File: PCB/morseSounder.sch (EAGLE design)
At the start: 51 parts, among them IC1 LM386N-1, IC2 LM324N, IC3 MAT-02H, Q1 2N3904

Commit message: Added avr based keyer and key input stages
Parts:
- added IC4: AVR-MEGA8-PPTH, SparkFun:AVR-MEGA8-PPTH
- added J1: AVR_SPI_PRG_6PTH, SparkFun:AVR_SPI_PRG_6PTH
- added JP1, JP3, JP4: JUMPER-3SMD, SparkFun:JUMPER-3SMD
- added LED1, LED2, LED3: (no value), SparkFun:LED-3MM-NO_SILK
- added OK2, OK3: 4N35, optocoupler:4N35
- added R27, R28, R29: 750, SparkFun:RESISTOR0805-RES
- added S1: (no value), SparkFun:SWITCH-SPSTSMD2
- added U$4: MOUNTSPKR_20*40, morseSounder:MOUNTSPKR_20*40
- added U$6: P082DTH, morseSounder:P082DTH
- added X1: (no value), con-molex:KK-156-2
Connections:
- net N$10 renamed KEY_IN
- new net ADC_RATE: IC4.PC1(ADC1), U$6G$1.S
- new net ADC_WEIGHT: IC4.PC0(ADC0), U$6G$2.S
- new net AVR_DASH: IC4.PC3(ADC3)
- new net AVR_DOT: IC4.PC2(ADC2)
- new net AVR_KEY_DASH: OK3.COL
- new net AVR_KEY_DOT: OK2.COL
- new net AVR_KEY_MODE: IC4.PC5(ADC5/SCL), S1.P
- new net AVR_KEY_OUT: IC4.PC4(ADC4/SDA), JP4.1
- new net AVR_MISO: IC4.PB4(MISO), J1.1
- new net AVR_MOSI: IC4.PB3(MOSI/OC2), J1.4
- new net AVR_RESET: IC4.PC6(/RESET), J1.5
- new net AVR_RX: IC4.PD0(RXD)
- new net AVR_SCK: IC4.PB5(SCK), J1.3
- new net AVR_TX: IC4.PD1(TXD)
- new net AVR_VCC: IC4.AREF, IC4.AVCC, IC4.VCC@1, J1.2, R28.2, R29.2, U$6G$1.E, U$6G$2.E
- new net KEY_DASH: JP3.3, OK3.C, U$1.RING
- new net KEY_DOT: JP3.1, OK2.C, U$1.TIP
- new net KEY_INPUT: JP1.1, JP3.2
- new net N$10: LED1.C, OK1.A
- new net N$28: U$2.TN, X1-1.S
- new net N$29: LED3.A, R29.1
- new net N$30: JP4.2, R27.2
- new net N$31: JP1.2, OK1.C
- new net N$32: LED1.A, R27.1
- new net N$33: LED2.A, R28.1
- new net N$34: LED2.C, OK3.A
- new net N$35: LED3.C, OK2.A
- net +12V: now also JP4.3
- net GND: now also IC4.AGND, IC4.GND@1, J1.6, JP1.3, OK2.EMI, OK3.EMI, S1.S, U$6G$1.A, U$6G$2.A, X1-2.S
- net N$2: now also U$2.RING
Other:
- note added: "AVR opto isolators"
- note added: "Internal speaker connector"
- note added: "Keyer IC and programming header"
- note added: "Keyer controls"
- note added: "Level translator and key input select"
- note added: "Rate"
- note added: "Weight"
- note added: "for keyer"
- note added: "for non keyer"
- note added: "non keyer Input selection"
- moved on the sheet: C1, C10, C11, C12, C13, C14, C15, C16, C2, C3, C4, C5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

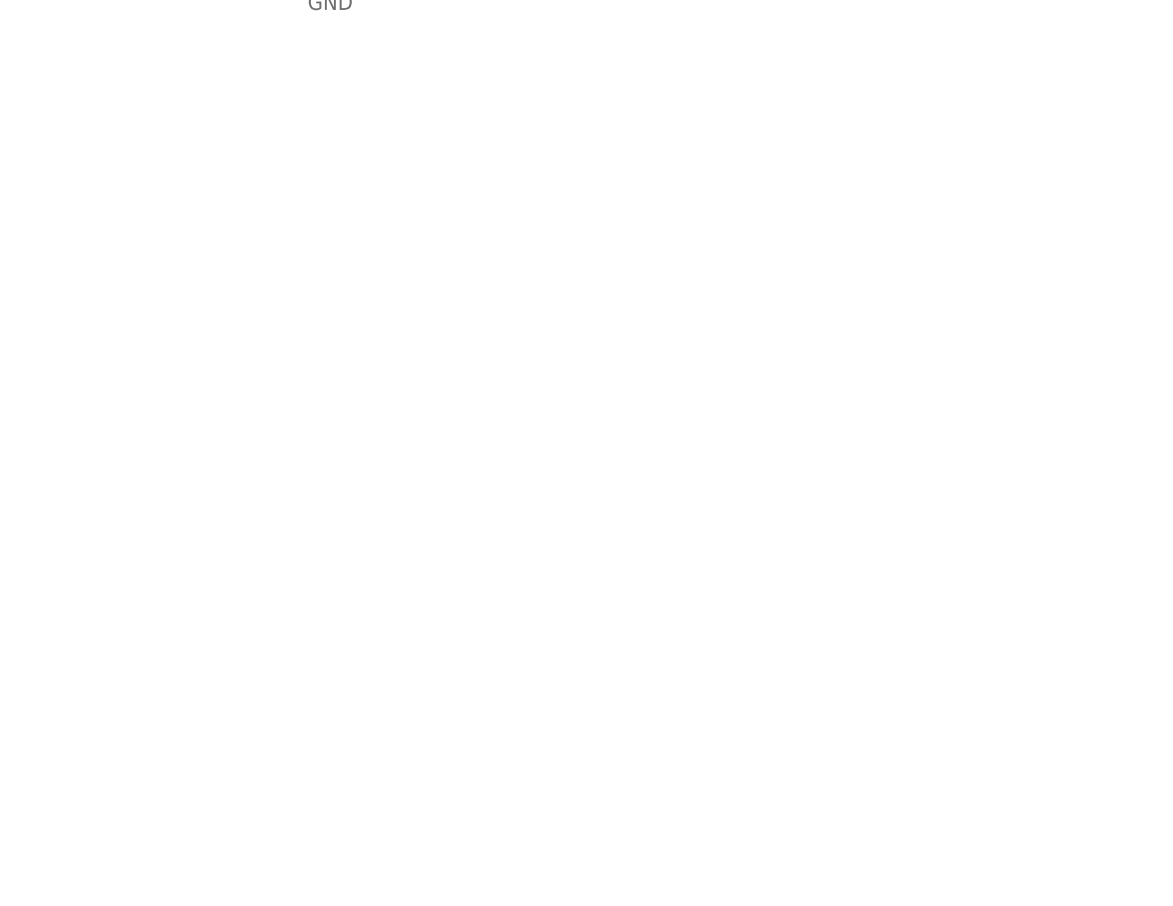
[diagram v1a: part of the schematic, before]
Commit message: Added power supply circuitry
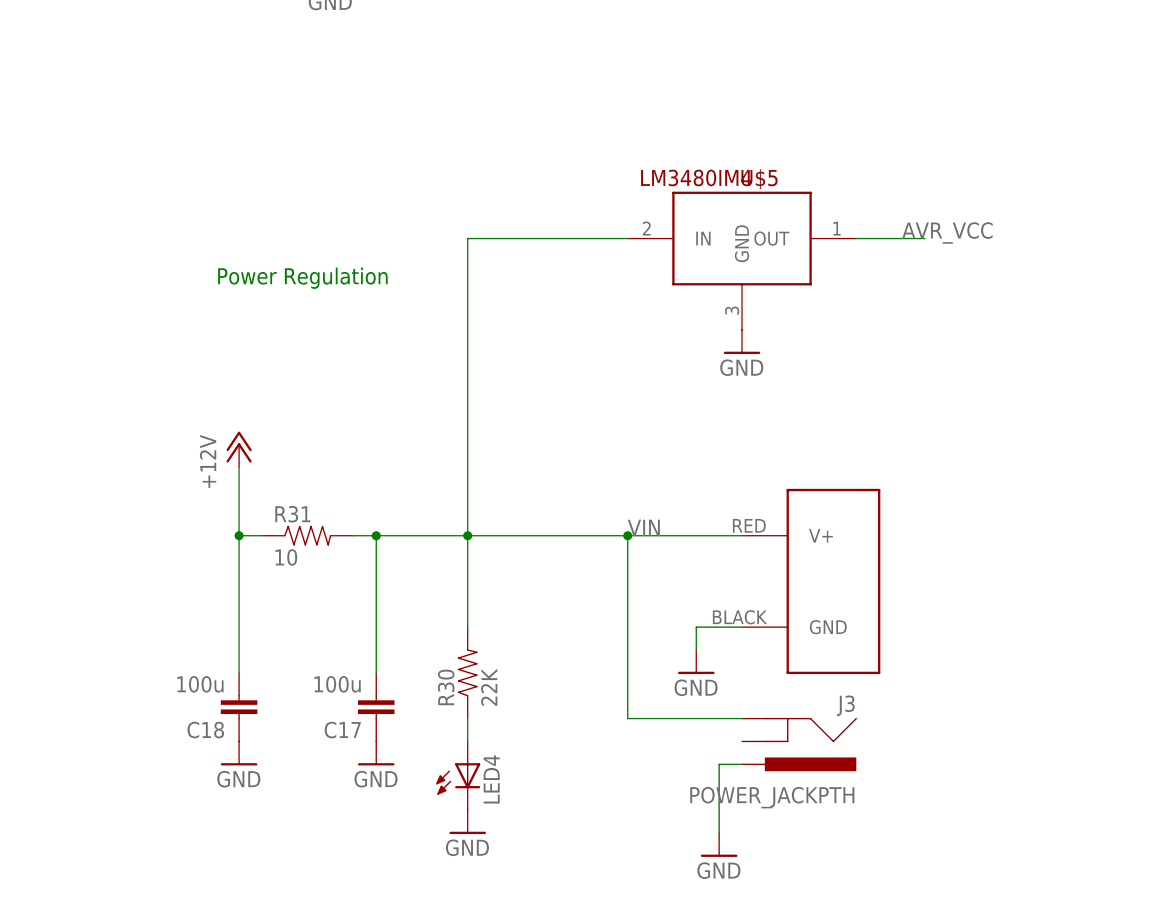
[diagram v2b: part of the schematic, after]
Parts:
- added C17, C18: 100u, SparkFun:CAP0805
- added J2: POWERPOLE_POWER25A_HORIZONTAL_G2, powerpoles:POWERPOLE_POWER25A_HORIZONTAL_G2
- added J3: POWER_JACKPTH, SparkFun:POWER_JACKPTH
- added LED4: (no value), SparkFun:LED-3MM-NO_SILK
- added R30: 22K, SparkFun:RESISTOR0805-RES
- added R31: 10, SparkFun:RESISTOR0805-RES
- added U$5: LM3480IM4, SparkFun-PowerIC:LM3480IM4
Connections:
- new net N$36: LED4.A, R30.1
- new net VIN: C17.2, J2.V+, J3.GND, R30.2, R31.2, U$5.IN
- net +12V: now also C18.2, R31.1
- net AVR_VCC: now also U$5.OUT
- net GND: now also C17.1, C18.1, J2.GND, J3.PWR, LED4.C, U$5.GND
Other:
- note added: "Power Regulation"
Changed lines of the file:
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@@
 <layer number="56" name="wert" color="7" fill="1" visible="no" active="no"/>
 <layer number="57" name="tCAD" color="7" fill="1" visible="no" active="no"/>
+<layer number="90" name="Modules" color="5" fill="1" visible="yes" active="yes"/>
 <layer number="91" name="Nets" color="2" fill="1" visible="yes" active="yes"/>
 <layer number="92" name="Busses" color="1" fill="1" visible="yes" active="yes"/>
@@
 <layer number="251" name="SMDround" color="12" fill="11" visible="no" active="no"/>
 <layer number="254" name="cooling" color="7" fill="1" visible="no" active="yes"/>
+<layer number="255" name="routoute" color="7" fill="1" visible="yes" active="yes"/>
 </layers>
 <schematic xreflabel="%F%N/%S.%C%R" xrefpart="/%S.%C%R">
@@
 <part name="S1" library="SparkFun" deviceset="SWITCH-SPST" device="SMD2"/>
 <part name="GND24" library="supply1" deviceset="GND" device=""/>
+<part name="U$5" library="SparkFun-PowerIC" deviceset="LM3480IM4" device=""/>
+<part name="J2" library="powerpoles" deviceset="POWERPOLE_POWER" device="25A_HORIZONTAL_G2"/>
+<part name="J3" library="SparkFun" deviceset="POWER_JACK" device="PTH"/>
+<part name="GND25" library="supply1" deviceset="GND" device=""/>
+<part name="GND26" library="supply1" deviceset="GND" device=""/>
+<part name="R30" library="SparkFun" deviceset="RESISTOR" device="0805-RES" value="22K"/>
+<part name="LED4" library="SparkFun" deviceset="LED" device="-3MM-NO_SILK"/>
+<part name="GND27" library="supply1" deviceset="GND" device=""/>
+<part name="R31" library="SparkFun" deviceset="RESISTOR" device="0805-RES" value="10"/>
+<part name="GND28" library="supply1" deviceset="GND" device=""/>
+<part name="C17" library="SparkFun" deviceset="CAP" device="0805" value="100u"/>
+<part name="C18" library="SparkFun" deviceset="CAP" device="0805" value="100u"/>
+<part name="GND29" library="supply1" deviceset="GND" device=""/>
+<part name="GND30" library="supply1" deviceset="GND" device=""/>
+<part name="P+9" library="supply1" deviceset="+12V" device=""/>
 </parts>
 <sheets>
@@
 <text x="152.4" y="53.34" size="1.778" layer="91">for non keyer</text>
 <text x="142.24" y="175.26" size="1.778" layer="91">AVR opto isolators</text>
+<text x="287.02" y="0" size="1.778" layer="91">Power Regulation</text>
 </plain>
 <instances>
@@
 <instance part="S1" gate="1" x="35.56" y="236.22"/>
 <instance part="GND24" gate="1" x="40.64" y="231.14"/>
+<instance part="U$5" gate="G$1" x="345.44" y="5.08"/>
+<instance part="J2" gate="G$1" x="355.6" y="-33.02"/>
+<instance part="J3" gate="G$1" x="347.98" y="-45.72" rot="R180"/>
+<instance part="GND25" gate="1" x="342.9" y="-63.5"/>
+<instance part="GND26" gate="1" x="340.36" y="-43.18"/>
+<instance part="R30" gate="G$1" x="314.96" y="-43.18" rot="R90"/>
+<instance part="LED4" gate="G$1" x="314.96" y="-53.34"/>
+<instance part="GND27" gate="1" x="314.96" y="-60.96"/>
+<instance part="R31" gate="G$1" x="297.18" y="-27.94"/>
+<instance part="GND28" gate="1" x="345.44" y="-7.62"/>
+<instance part="C17" gate="G$1" x="304.8" y="-45.72" rot="R180"/>
+<instance part="C18" gate="G$1" x="289.56" y="-45.72" rot="R180"/>
+<instance part="GND29" gate="1" x="304.8" y="-53.34"/>
+<instance part="GND30" gate="1" x="289.56" y="-53.34"/>
+<instance part="P+9" gate="1" x="289.56" y="-17.78"/>
 </instances>
 <busses>
@@
 <pinref part="GND24" gate="1" pin="GND"/>
 </segment>
+<segment>
+<pinref part="J2" gate="G$1" pin="GND"/>
+<wire x1="345.44" y1="-38.1" x2="340.36" y2="-38.1" width="0.1524" layer="91"/>
+<pinref part="GND26" gate="1" pin="GND"/>
+<wire x1="340.36" y1="-38.1" x2="340.36" y2="-40.64" width="0.1524" layer="91"/>
+</segment>
+<segment>
+<pinref part="J3" gate="G$1" pin="PWR"/>
+<wire x1="345.44" y1="-53.34" x2="342.9" y2="-53.34" width="0.1524" layer="91"/>
+<pinref part="GND25" gate="1" pin="GND"/>
+<wire x1="342.9" y1="-53.34" x2="342.9" y2="-60.96" width="0.1524" layer="91"/>
+</segment>
+<segment>
+<pinref part="LED4" gate="G$1" pin="C"/>
+<pinref part="GND27" gate="1" pin="GND"/>
+</segment>
+<segment>
+<pinref part="U$5" gate="G$1" pin="GND"/>
+<pinref part="GND28" gate="1" pin="GND"/>
+</segment>
+<segment>
+<pinref part="C17" gate="G$1" pin="1"/>
+<pinref part="GND29" gate="1" pin="GND"/>
+</segment>
+<segment>
+<pinref part="C18" gate="G$1" pin="1"/>
+<pinref part="GND30" gate="1" pin="GND"/>
+</segment>
 </net>
 <net name="AUDIO_OUT" class="0">
@@
 <pinref part="JP4" gate="G$1" pin="3"/>
 <wire x1="172.72" y1="88.9" x2="167.64" y2="88.9" width="0.1524" layer="91"/>
+</segment>
+<segment>
+<pinref part="R31" gate="G$1" pin="1"/>
+<wire x1="292.1" y1="-27.94" x2="289.56" y2="-27.94" width="0.1524" layer="91"/>
+<pinref part="C18" gate="G$1" pin="2"/>
+<wire x1="289.56" y1="-27.94" x2="289.56" y2="-43.18" width="0.1524" layer="91"/>
+<pinref part="P+9" gate="1" pin="+12V"/>
+<wire x1="289.56" y1="-27.94" x2="289.56" y2="-20.32" width="0.1524" layer="91"/>
+<junction x="289.56" y="-27.94"/>
 </segment>
 </net>
@@
 <label x="40.64" y="241.3" size="1.778" layer="95" rot="R90"/>
 </segment>
+<segment>
+<pinref part="U$5" gate="G$1" pin="OUT"/>
+<wire x1="358.14" y1="5.08" x2="365.76" y2="5.08" width="0.1524" layer="91"/>
+<label x="363.22" y="5.08" size="1.778" layer="95"/>
+</segment>
 </net>
 <net name="ADC_RATE" class="0">
@@
 </segment>
 </net>
+<net name="VIN" class="0">
+<segment>
+<pinref part="J3" gate="G$1" pin="GND"/>
+<wire x1="345.44" y1="-48.26" x2="332.74" y2="-48.26" width="0.1524" layer="91"/>
+<wire x1="332.74" y1="-48.26" x2="332.74" y2="-27.94" width="0.1524" layer="91"/>
+<pinref part="J2" gate="G$1" pin="V+"/>
+<wire x1="332.74" y1="-27.94" x2="345.44" y2="-27.94" width="0.1524" layer="91"/>
+<wire x1="332.74" y1="-27.94" x2="314.96" y2="-27.94" width="0.1524" layer="91"/>
+<label x="332.74" y="-27.94" size="1.778" layer="95"/>
+<junction x="332.74" y="-27.94"/>
+<pinref part="R30" gate="G$1" pin="2"/>
+<wire x1="314.96" y1="-38.1" x2="314.96" y2="-27.94" width="0.1524" layer="91"/>
+<pinref part="U$5" gate="G$1" pin="IN"/>
+<wire x1="314.96" y1="-27.94" x2="314.96" y2="5.08" width="0.1524" layer="91"/>
+<wire x1="314.96" y1="5.08" x2="332.74" y2="5.08" width="0.1524" layer="91"/>
+<pinref part="R31" gate="G$1" pin="2"/>
+<wire x1="314.96" y1="-27.94" x2="304.8" y2="-27.94" width="0.1524" layer="91"/>
+<junction x="314.96" y="-27.94"/>
+<pinref part="C17" gate="G$1" pin="2"/>
+<wire x1="304.8" y1="-43.18" x2="304.8" y2="-27.94" width="0.1524" layer="91"/>
+<wire x1="304.8" y1="-27.94" x2="302.26" y2="-27.94" width="0.1524" layer="91"/>
+<junction x="304.8" y="-27.94"/>
+</segment>
+</net>
+<net name="N$36" class="0">
+<segment>
+<pinref part="R30" gate="G$1" pin="1"/>
+<pinref part="LED4" gate="G$1" pin="A"/>
+<wire x1="314.96" y1="-48.26" x2="314.96" y2="-50.8" width="0.1524" layer="91"/>
+</segment>
+</net>

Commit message: Added Touch keyer circuit and initial board
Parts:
- added C19, C20: 100n, SparkFun:CAP0805
- added JP2: (no value), SparkFun:M03POLAR
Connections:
- net AVR_RX: now also JP2.1
- net AVR_TX: now also JP2.2
- net AVR_VCC: now also C20.1
- net GND: now also C19.2, C20.2, JP2.3
- net VIN: now also C19.1
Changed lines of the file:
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@@
 <part name="GND30" library="supply1" deviceset="GND" device=""/>
 <part name="P+9" library="supply1" deviceset="+12V" device=""/>
+<part name="JP2" library="SparkFun" deviceset="M03" device="POLAR"/>
+<part name="GND31" library="supply1" deviceset="GND" device=""/>
+<part name="C19" library="SparkFun" deviceset="CAP" device="0805" value="100n"/>
+<part name="C20" library="SparkFun" deviceset="CAP" device="0805" value="100n"/>
+<part name="GND32" library="supply1" deviceset="GND" device=""/>
+<part name="GND33" library="supply1" deviceset="GND" device=""/>
 </parts>
 <sheets>
@@
 <instance part="GND30" gate="1" x="289.56" y="-53.34"/>
 <instance part="P+9" gate="1" x="289.56" y="-17.78"/>
+<instance part="JP2" gate="G$1" x="-17.78" y="147.32"/>
+<instance part="GND31" gate="1" x="7.62" y="147.32"/>
+<instance part="C19" gate="G$1" x="325.12" y="0"/>
+<instance part="C20" gate="G$1" x="360.68" y="0"/>
+<instance part="GND32" gate="1" x="325.12" y="-5.08"/>
+<instance part="GND33" gate="1" x="360.68" y="-5.08"/>
 </instances>
 <busses>
@@
 <pinref part="C18" gate="G$1" pin="1"/>
 <pinref part="GND30" gate="1" pin="GND"/>
+</segment>
+<segment>
+<pinref part="JP2" gate="G$1" pin="3"/>
+<wire x1="-10.16" y1="149.86" x2="7.62" y2="149.86" width="0.1524" layer="91"/>
+<pinref part="GND31" gate="1" pin="GND"/>
+</segment>
+<segment>
+<pinref part="C19" gate="G$1" pin="2"/>
+<pinref part="GND32" gate="1" pin="GND"/>
+</segment>
+<segment>
+<pinref part="C20" gate="G$1" pin="2"/>
+<pinref part="GND33" gate="1" pin="GND"/>
 </segment>
 </net>
@@
 <segment>
 <pinref part="U$5" gate="G$1" pin="OUT"/>
-<wire x1="358.14" y1="5.08" x2="365.76" y2="5.08" width="0.1524" layer="91"/>
+<wire x1="358.14" y1="5.08" x2="360.68" y2="5.08" width="0.1524" layer="91"/>
 <label x="363.22" y="5.08" size="1.778" layer="95"/>
+<pinref part="C20" gate="G$1" pin="1"/>
+<wire x1="360.68" y1="5.08" x2="365.76" y2="5.08" width="0.1524" layer="91"/>
+<junction x="360.68" y="5.08"/>
 </segment>
 </net>
@@
 <label x="93.98" y="154.94" size="1.778" layer="95"/>
 </segment>
+<segment>
+<pinref part="JP2" gate="G$1" pin="1"/>
+<wire x1="-10.16" y1="144.78" x2="0" y2="144.78" width="0.1524" layer="91"/>
+<label x="-7.62" y="144.78" size="1.778" layer="95"/>
+</segment>
 </net>
 <net name="AVR_TX" class="0">
@@
 <wire x1="88.9" y1="152.4" x2="99.06" y2="152.4" width="0.1524" layer="91"/>
 <label x="93.98" y="152.4" size="1.778" layer="95"/>
+</segment>
+<segment>
+<pinref part="JP2" gate="G$1" pin="2"/>
+<wire x1="-10.16" y1="147.32" x2="0" y2="147.32" width="0.1524" layer="91"/>
+<label x="-7.62" y="147.32" size="1.778" layer="95"/>
 </segment>
 </net>
@@
 <pinref part="U$5" gate="G$1" pin="IN"/>
 <wire x1="314.96" y1="-27.94" x2="314.96" y2="5.08" width="0.1524" layer="91"/>
-<wire x1="314.96" y1="5.08" x2="332.74" y2="5.08" width="0.1524" layer="91"/>
+<wire x1="314.96" y1="5.08" x2="325.12" y2="5.08" width="0.1524" layer="91"/>
 <pinref part="R31" gate="G$1" pin="2"/>
+<wire x1="325.12" y1="5.08" x2="332.74" y2="5.08" width="0.1524" layer="91"/>
 <wire x1="314.96" y1="-27.94" x2="304.8" y2="-27.94" width="0.1524" layer="91"/>
 <junction x="314.96" y="-27.94"/>
@@
 <wire x1="304.8" y1="-27.94" x2="302.26" y2="-27.94" width="0.1524" layer="91"/>
 <junction x="304.8" y="-27.94"/>
-</segment>
-</net>
+<pinref part="C19" gate="G$1" pin="1"/>
+<junction x="325.12" y="5.08"/>
+</segment>
+</net>

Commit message: optimized schematic components and added initial board file
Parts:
- removed C10, C11: 10n, SparkFun:CAP0805
- removed C12: 100u, SparkFun:CAP0805
- removed C8: 100n, SparkFun:CAP0805
- removed C9: 20n, SparkFun:CAP0805
- removed IC2: LM324N, linear:LM324N
- removed R16, R22, R23: 10K, SparkFun:RESISTOR0805-RES
- removed R17, R18: 33K, SparkFun:RESISTOR0805-RES
- removed R19, R20: 100K, SparkFun:RESISTOR0805-RES
- removed R21: 47K, SparkFun:RESISTOR0805-RES
- added IC5: LM321MF, linear:LM321MF
- added IC6: MEGA16-A, atmel:MEGA16-A
- IC1: value LM386N-1 -> LM386M-1; device linear:LM386N-1 -> linear:LM386M-1
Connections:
- removed net N$14: C8.1, C9.2, IC2B.-IN, IC2B.OUT
- removed net N$15: C8.2, R16.1
- removed net N$16: C11.2, IC2C.OUT, R18.1, R21.2
- removed net N$17: C10.1, IC2B.+IN, R17.2
- removed net N$18: C9.1, R17.1, R18.2
- removed net N$19: C11.1, IC2C.-IN, R19.2
- removed net N$20: IC2D.OUT, R19.1, R20.2
- removed net N$21: IC2D.-IN, R20.1, R21.1
- removed net N$22: C12.2, IC2C.+IN, IC2D.+IN, R22.2, R23.1
- removed net N$27: C16.2
- net +12V: now also IC5.V+; no longer IC2P.V+, R22.1
- net GND: now also IC5.V-, J3.GND, U$3G$1.S, U$3G$2.A; no longer C10.2, C12.1, IC2P.V-, J3.PWR, R23.2, U$3G$1.A, U$3G$2.S
- net N$26: now also U$3G$1.A; no longer U$3G$2.A
- net N$4: now also U$3G$2.E, U$3G$2.S; no longer U$3G$1.E, U$3G$1.S
- net N$5: now also IC5.OUT; no longer IC2A.OUT
- net N$6: now also IC5.-IN; no longer IC2A.-IN
- net N$7: now also IC5.+IN; no longer IC2A.+IN
- net TONE_OUT: now also C16.2; no longer R16.2
- net VIN: now also J3.PWR; no longer J3.GND
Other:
- note removed: "LM324N power"
- note removed: "Low pass filter"
- note removed: "Wave Generator"
- moved on the sheet: C4, C5, C6, J3, R10, R3, R4, R5, R6, R9, U$3G$1, U$3G$2

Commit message: Replaced most through hole components with SMD equivilents
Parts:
- removed IC3: MAT-02H, linear:MAT-02H
- removed IC4: AVR-MEGA8-PPTH, SparkFun:AVR-MEGA8-PPTH
- removed IC6: MEGA16-A, atmel:MEGA16-A
- added Q2, Q3: MMBT3904, transistor:MMBT3904LT1-NPN-SOT23-BEC
- added R16: 10K, SparkFun:RESISTOR0805-RES
- added SJ1: SOLDERJUMPERNO, SparkFun:SOLDERJUMPERNO
- added U1: ATMEGA168, SparkFun:ATMEGA168
- Q1: value 2N3904 -> MMBT3904; device transistor-npn:2N3904 -> transistor:MMBT3904LT1-NPN-SOT23-BEC
- T1: value (none) -> MMBTA42; device transistor:MPSA42-NPN-TO92-EBC -> SparkFun:TRANSISTOR_NPNSOT23
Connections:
- new net N$14: SJ1.2, U$2.RING
- net ADC_RATE: now also U1.PC1(ADC1); no longer IC4.PC1(ADC1)
- net ADC_WEIGHT: now also U1.PC0(ADC0); no longer IC4.PC0(ADC0)
- net AVR_DASH: now also U1.PC3(ADC3); no longer IC4.PC3(ADC3)
- net AVR_DOT: now also U1.PC2(ADC2); no longer IC4.PC2(ADC2)
- net AVR_KEY_MODE: now also R16.2, U1.PC5(ADC5/SCL); no longer IC4.PC5(ADC5/SCL)
- net AVR_KEY_OUT: now also U1.PC4(ADC4/SDA); no longer IC4.PC4(ADC4/SDA)
- net AVR_MISO: now also U1.PB4(MISO); no longer IC4.PB4(MISO)
- net AVR_MOSI: now also U1.PB3(MOSI/OC2); no longer IC4.PB3(MOSI/OC2)
- net AVR_RESET: now also U1.PC6(/RESET); no longer IC4.PC6(/RESET)
- net AVR_RX: now also U1.PD0(RXD); no longer IC4.PD0(RXD)
- net AVR_SCK: now also U1.PB5(SCK); no longer IC4.PB5(SCK)
- net AVR_TX: now also U1.PD1(TXD); no longer IC4.PD1(TXD)
- net AVR_VCC: now also R16.1, U1.AREF, U1.AVCC, U1.VCC@1, U1.VCC@2; no longer IC4.AREF, IC4.AVCC, IC4.VCC@1
- net GND: now also U1.AGND, U1.GND@1, U1.GND@2; no longer IC4.AGND, IC4.GND@1
- net N$11: now also Q3.B; no longer IC3B.B
- net N$2: now also SJ1.1; no longer U$2.RING
- net N$6: now also Q2.C; no longer IC3A.C
- net N$7: now also Q3.C; no longer IC3B.C
- net N$8: now also Q2.E, Q3.E; no longer IC3A.E, IC3B.E
- net TONE_OUT: now also Q2.B; no longer IC3A.B
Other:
- note added: "Short for stereo opperation"
- moved on the sheet: C1, C3

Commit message: Added test points and cleaned up some silkscreen issues
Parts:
- removed X1: (no value), con-molex:KK-156-2
- added J4: (no value), SparkFun-Connectors:CONN_02
- added TP1, TP2, TP3, TP4, TP5, TP6, TP7, TP8: TEST-POINT3X5, SparkFun-Connectors:TEST-POINT3X5
- JP2: device SparkFun:M03POLAR -> SparkFun-Connectors:CONN_03
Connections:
- removed net N$4: R2.2, R3.2, U$3G$2.E, U$3G$2.S
- new net N$15: R2.2, R3.2, TP8.1, U$3G$2.E, U$3G$2.S
- net ADC_RATE: now also TP1.1
- net ADC_WEIGHT: now also TP2.1
- net AUDIO_OUT: now also TP4.1
- net AUDIO_PRE_AMP: now also TP5.1
- net AVR_KEY_MODE: now also TP3.1
- net GND: now also J4.2; no longer X1-2.S
- net KEY_IN: now also TP7.1
- net N$28: now also J4.1; no longer X1-1.S
- net TONE_OUT: now also TP6.1
